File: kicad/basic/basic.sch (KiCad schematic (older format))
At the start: 20 parts, among them P2 CONN_01X15, P3 CONN_01X15, P4 CONN_01X06, P5 CONN_01X01, P6 CONN_01X01, P7 CONN_01X01, P8 CONN_01X01, P9 CONN_01X06, SW1 SW_PUSH, SW2 SW_PUSH

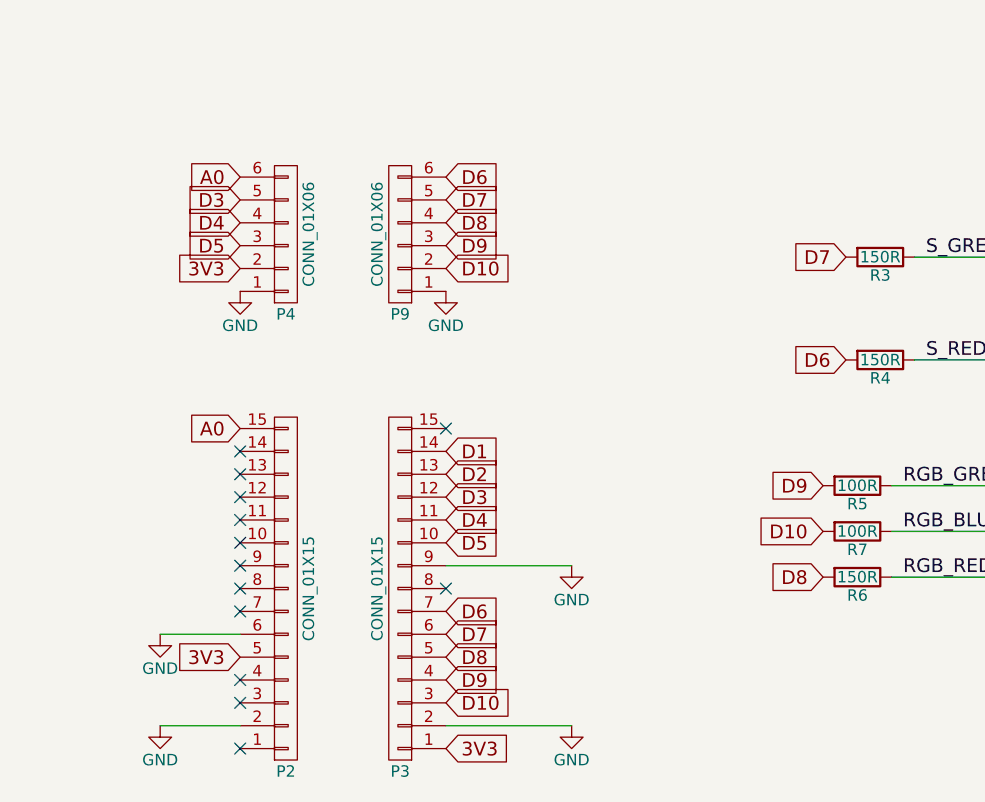
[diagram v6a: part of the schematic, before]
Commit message: Changed pin assignments
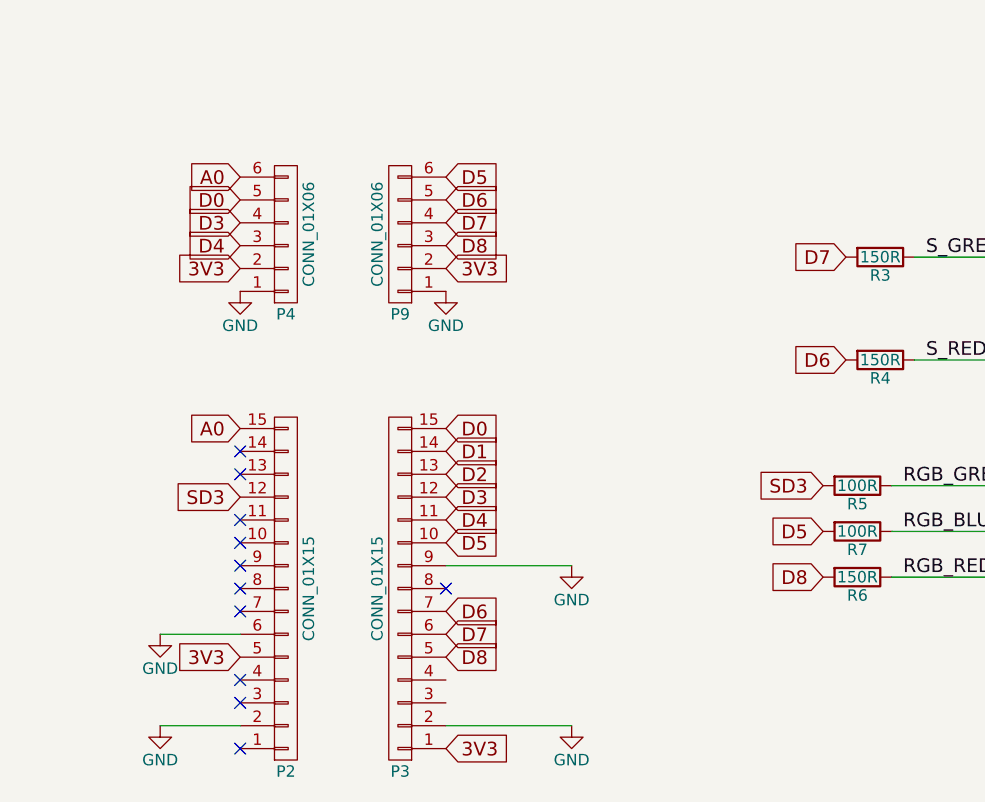
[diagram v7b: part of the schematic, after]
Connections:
- net 3V3: now also P9.2 (P2)
- net D3: now also P4.4 (P4); no longer P4.5 (P5)
- net D4: now also P4.3 (P3); no longer P4.4 (P4)
- net D5: now also P9.6 (P6), R7.2; no longer P4.3 (P3)
- net D6: now also P9.5 (P5); no longer P9.6 (P6)
- net D7: now also P9.4 (P4); no longer P9.5 (P5)
- net D8: now also P9.3 (P3); no longer P9.4 (P4)
- net SD3: now reaches P2.12 (P12)
- net SD3: now also R5.2
- net D0: now reaches P3.15 (P15)
- net D0: now also P4.5 (P5)
- removed net D10: P3.3 (P3), P9.2 (P2), R7.2
- removed net D9: P3.4 (P4), P9.3 (P3), R5.2
- no-connect marks 13 -> 11
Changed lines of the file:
@@
 Text GLabel 5500 2400 0    60   Input ~ 0
 A0
-Text GLabel 6400 4700 2    60   Input ~ 0
-D10
 Text GLabel 6400 3800 2    60   Input ~ 0
 D3
-Text GLabel 6400 4600 2    60   Input ~ 0
-D9
 Text GLabel 6400 4500 2    60   Input ~ 0
 D8
@@
 Wire Wire Line
 	6400 4100 6950 4100
-NoConn ~ 6400 3500
 NoConn ~ 5500 3600
 NoConn ~ 5500 3700
-NoConn ~ 5500 3800
 NoConn ~ 5500 3900
 NoConn ~ 5500 4000
@@
 	1    0    0    -1
 $EndComp
-Text GLabel 6400 2800 2    60   Input ~ 0
-D10
 Text GLabel 6400 2700 2    60   Input ~ 0
-D9
+D8
 Text GLabel 6400 2600 2    60   Input ~ 0
-D8
-Text GLabel 6400 2500 2    60   Input ~ 0
 D7
 Text GLabel 6400 2400 2    60   Input ~ 0
-D6
-Text GLabel 5500 2500 0    60   Input ~ 0
+D5
+Text GLabel 5500 2600 0    60   Input ~ 0
 D3
-Text GLabel 5500 2600 0    60   Input ~ 0
+Text GLabel 5500 2700 0    60   Input ~ 0
 D4
 NoConn ~ 6400 4200
+Text GLabel 8050 3750 0    60   Input ~ 0
+SD3
 Text GLabel 8050 3950 0    60   Input ~ 0
-D10
-Text GLabel 8050 3750 0    60   Input ~ 0
-D9
+D5
 Text GLabel 8050 4150 0    60   Input ~ 0
 D8
@@
 Text GLabel 6400 4000 2    60   Input ~ 0
 D5
-Text GLabel 5500 2700 0    60   Input ~ 0
-D5
+Text GLabel 5500 2500 0    60   Input ~ 0
+D0
 Text GLabel 5500 2800 0    60   Input ~ 0
 3V3
@@
 Text Label 8500 3200 0    60   ~ 0
 S_RED
+Text GLabel 6400 2500 2    60   Input ~ 0
+D6
+Text GLabel 5500 3800 0    60   Input ~ 0
+SD3
+Text GLabel 6400 3500 2    60   Input ~ 0
+D0
+Text GLabel 6400 2800 2    60   Input ~ 0
+3V3
 $EndSCHEMATC

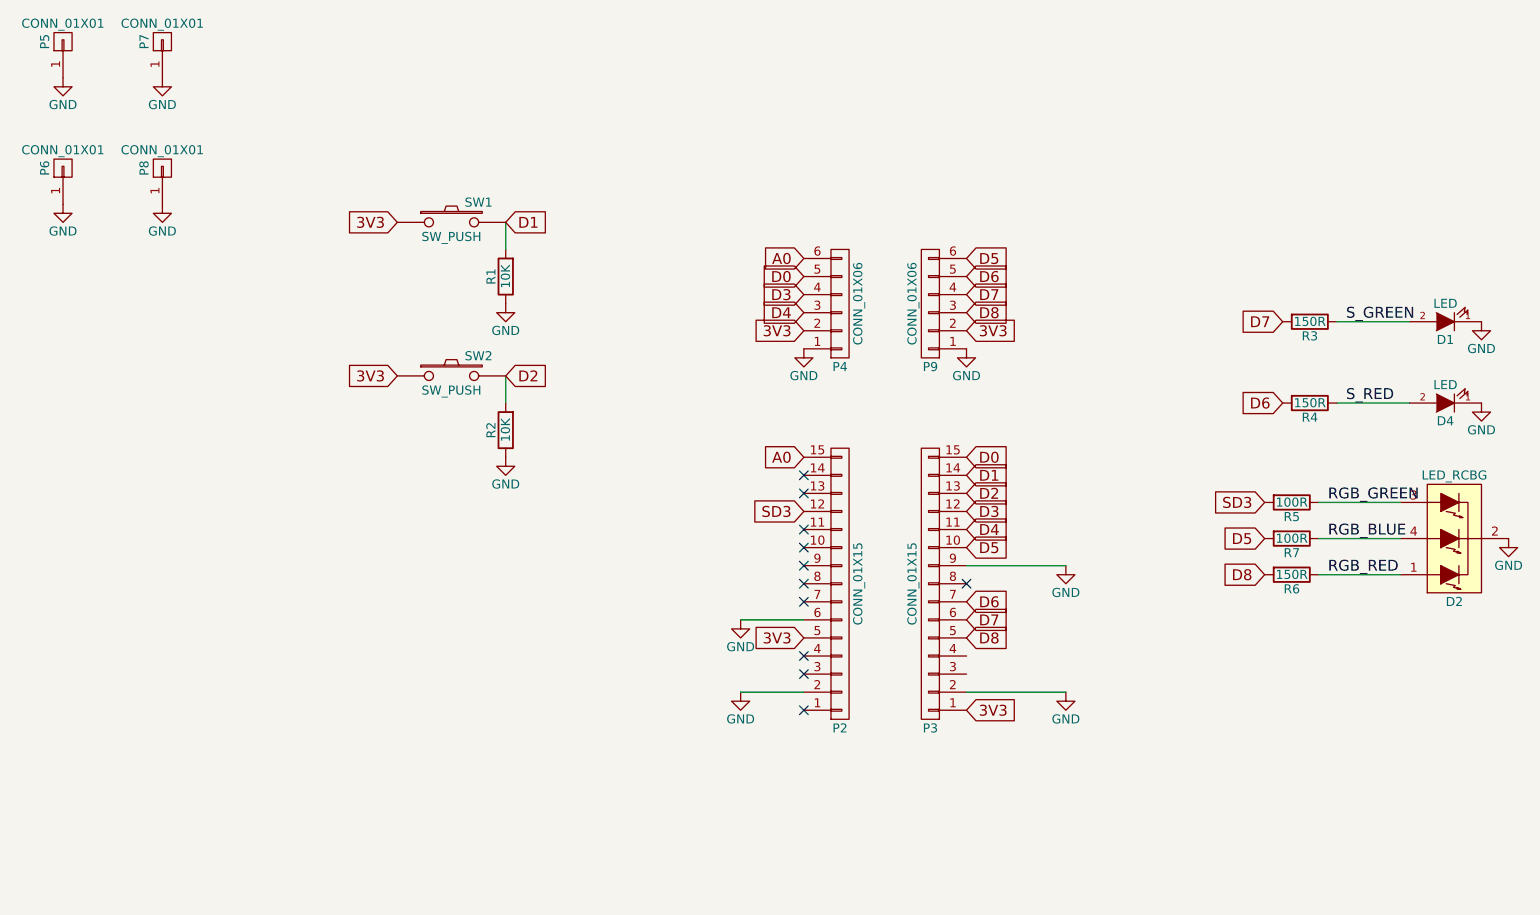
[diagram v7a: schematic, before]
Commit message: Use arduino pin numbers & breakout I2C & SPI
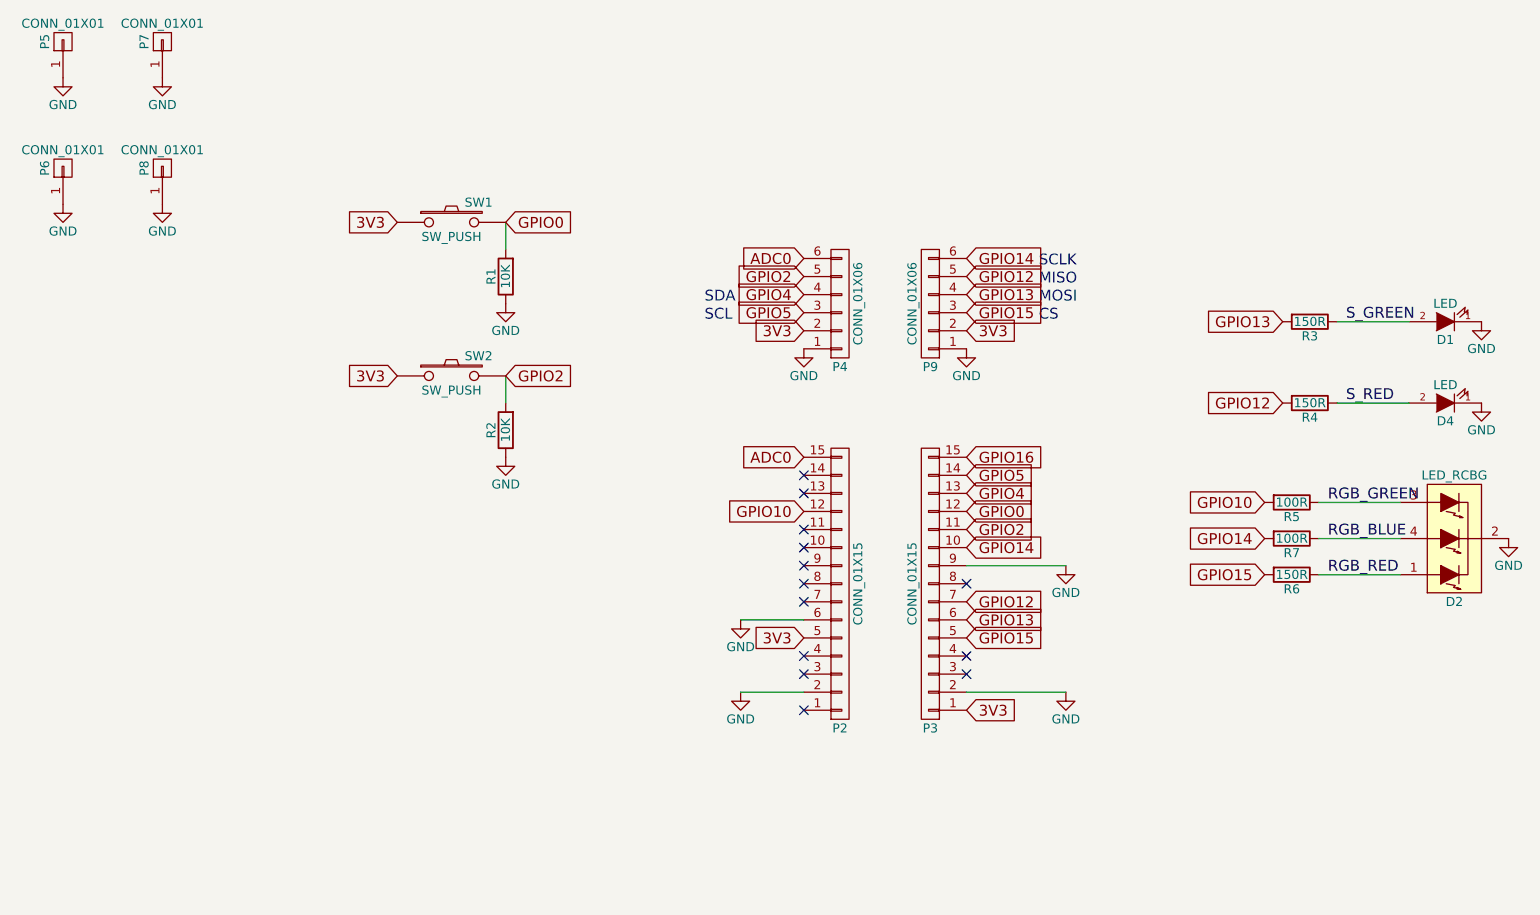
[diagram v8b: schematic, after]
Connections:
- net A0 renamed ADC0
- net D0 renamed GPIO16
- net GPIO16: no longer P4.5 (P5)
- net D1 renamed GPIO0
- net GPIO0: now also P3.12 (P12); no longer P3.14 (P14)
- net D2 renamed GPIO2
- net GPIO2: now also P3.11 (P11), P4.5 (P5); no longer P3.13 (P13)
- net D3 renamed GPIO4
- net GPIO4: now also P3.13 (P13); no longer P3.12 (P12)
- net D4 renamed GPIO5
- net GPIO5: now also P3.14 (P14); no longer P3.11 (P11)
- net D5 renamed GPIO14
- net D6 renamed GPIO12
- net D7 renamed GPIO13
- net D8 renamed GPIO15
- net SD3 renamed GPIO10
- no-connect marks 11 -> 13
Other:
- note added: "CS"
- note added: "MISO"
- note added: "MOSI"
- note added: "SCL"
- note added: "SCLK"
- note added: "SDA"
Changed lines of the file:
@@
 $EndComp
 Text GLabel 5500 3500 0    60   Input ~ 0
-A0
+ADC0
 Text GLabel 5500 2400 0    60   Input ~ 0
-A0
-Text GLabel 6400 3800 2    60   Input ~ 0
-D3
+ADC0
 Text GLabel 6400 4500 2    60   Input ~ 0
-D8
+GPIO15
 Text GLabel 6400 4400 2    60   Input ~ 0
-D7
+GPIO13
 Text GLabel 6400 4300 2    60   Input ~ 0
-D6
+GPIO12
 Text GLabel 6400 3900 2    60   Input ~ 0
-D4
-Text GLabel 6400 3700 2    60   Input ~ 0
-D2
-Text GLabel 6400 3600 2    60   Input ~ 0
-D1
+GPIO2
 Wire Wire Line
 	6400 4800 6950 4800
@@
 $EndComp
 Text GLabel 6400 2700 2    60   Input ~ 0
-D8
+GPIO15
 Text GLabel 6400 2600 2    60   Input ~ 0
-D7
+GPIO13
 Text GLabel 6400 2400 2    60   Input ~ 0
-D5
+GPIO14
 Text GLabel 5500 2600 0    60   Input ~ 0
-D3
+GPIO4
 Text GLabel 5500 2700 0    60   Input ~ 0
-D4
+GPIO5
 NoConn ~ 6400 4200
 Text GLabel 8050 3750 0    60   Input ~ 0
-SD3
+GPIO10
 Text GLabel 8050 3950 0    60   Input ~ 0
-D5
+GPIO14
 Text GLabel 8050 4150 0    60   Input ~ 0
-D8
+GPIO15
 Text GLabel 8150 2750 0    60   Input ~ 0
-D7
+GPIO13
 Text GLabel 3850 2200 2    60   Input ~ 0
-D1
+GPIO0
 Text GLabel 3850 3050 2    60   Input ~ 0
-D2
+GPIO2
 $Comp
 L LED_RCBG D2
@@
 $EndComp
 Text GLabel 8150 3200 0    60   Input ~ 0
-D6
+GPIO12
 $Comp
 L R R7
@@
 $EndComp
 Text GLabel 6400 4000 2    60   Input ~ 0
-D5
+GPIO14
 Text GLabel 5500 2500 0    60   Input ~ 0
-D0
+GPIO2
 Text GLabel 5500 2800 0    60   Input ~ 0
 3V3
@@
 S_RED
 Text GLabel 6400 2500 2    60   Input ~ 0
-D6
+GPIO12
 Text GLabel 5500 3800 0    60   Input ~ 0
-SD3
+GPIO10
 Text GLabel 6400 3500 2    60   Input ~ 0
-D0
+GPIO16
 Text GLabel 6400 2800 2    60   Input ~ 0
 3V3
+Text Notes 6800 2550 0    60   ~ 0
+MISO
+Text Notes 6800 2450 0    60   ~ 0
+SCLK
+Text Notes 6800 2650 0    60   ~ 0
+MOSI
+Text Notes 6800 2750 0    60   ~ 0
+CS
+Text Notes 4950 2650 0    60   ~ 0
+SDA
+Text Notes 4950 2750 0    60   ~ 0
+SCL
+Text GLabel 6400 3700 2    60   Input ~ 0
+GPIO4
+Text GLabel 6400 3600 2    60   Input ~ 0
+GPIO5
+Text GLabel 6400 3800 2    60   Input ~ 0
+GPIO0
+NoConn ~ 6400 4600
+NoConn ~ 6400 4700
 $EndSCHEMATC
